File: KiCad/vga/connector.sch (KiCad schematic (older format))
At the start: 13 parts, among them J1 DB15_Female_HighDensity_Mount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, X2 Edge72

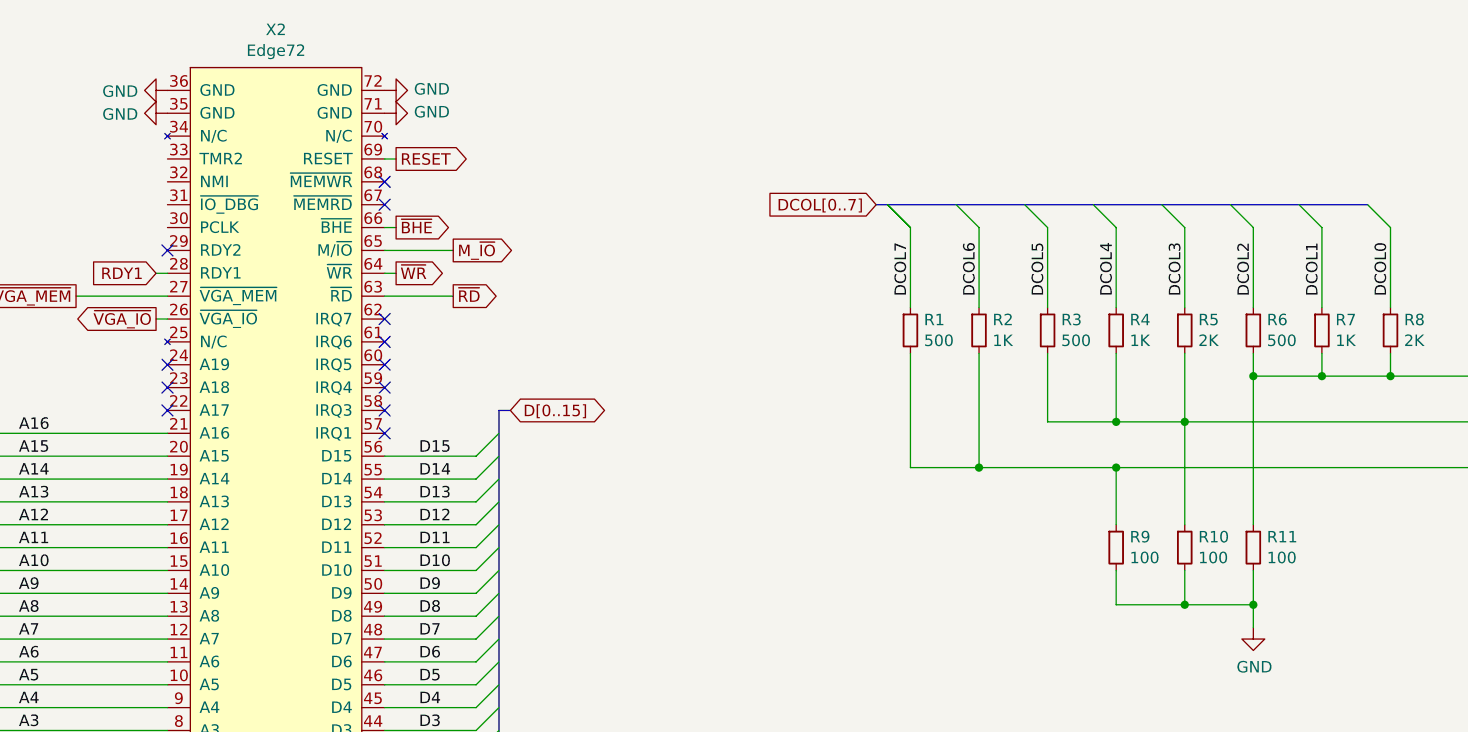
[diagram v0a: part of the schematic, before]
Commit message: Updated graphics adapter and main schematics + board.
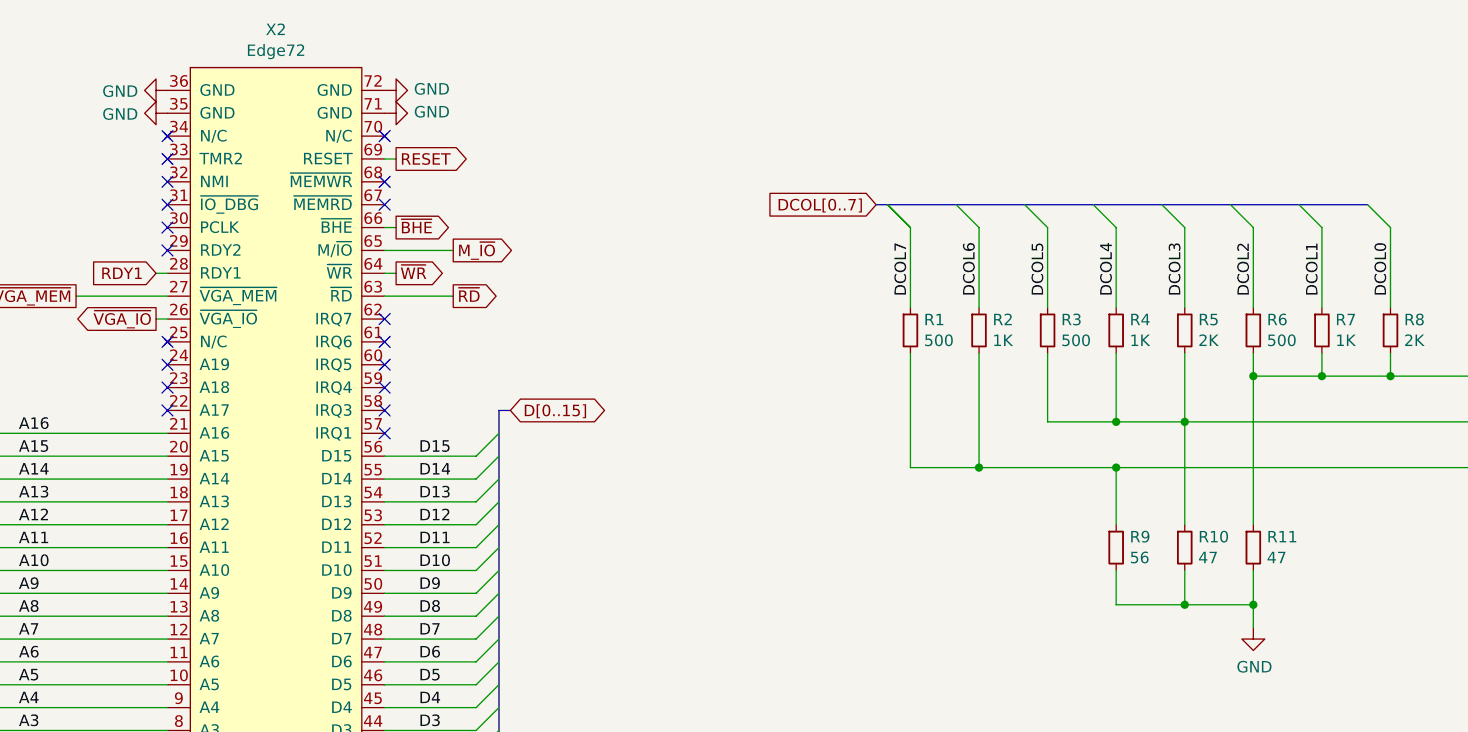
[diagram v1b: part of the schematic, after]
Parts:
- R10, R11: value 100 -> 47
- R9: value 100 -> 56
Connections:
- no-connect marks 18 -> 25
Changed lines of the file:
@@
 P 7000 4150
 F 0 "R9" H 7059 4196 50  0000 L CNN
-F 1 "100" H 7059 4105 50  0000 L CNN
+F 1 "56" H 7059 4105 50  0000 L CNN
 F 2 "Resistor_THT:R_Axial_DIN0204_L3.6mm_D1.6mm_P7.62mm_Horizontal" H 7000 4150 50  0001 C CNN
 F 3 "~" H 7000 4150 50  0001 C CNN
@@
 P 7300 4150
 F 0 "R10" H 7359 4196 50  0000 L CNN
-F 1 "100" H 7359 4105 50  0000 L CNN
+F 1 "47" H 7359 4105 50  0000 L CNN
 F 2 "Resistor_THT:R_Axial_DIN0204_L3.6mm_D1.6mm_P7.62mm_Horizontal" H 7300 4150 50  0001 C CNN
 F 3 "~" H 7300 4150 50  0001 C CNN
@@
 P 7600 4150
 F 0 "R11" H 7659 4196 50  0000 L CNN
-F 1 "100" H 7659 4105 50  0000 L CNN
+F 1 "47" H 7659 4105 50  0000 L CNN
 F 2 "Resistor_THT:R_Axial_DIN0204_L3.6mm_D1.6mm_P7.62mm_Horizontal" H 7600 4150 50  0001 C CNN
 F 3 "~" H 7600 4150 50  0001 C CNN
@@
 	1    0    0    -1
 $EndComp
-Wire Bus Line
-	5950 2650 8100 2650
-Wire Bus Line
-	2000 3400 2000 5150
-Wire Bus Line
-	4300 3550 4300 5150
 $Comp
 L Mini8086:Edge72 X2
 U 1 1 5F76D50A
 P 3300 3850
+AR Path="/5F76D50A" Ref="X2"  Part="1"
+AR Path="/5FB1662F/5F76D50A" Ref="X2"  Part="1"
 F 0 "X2" H 3325 5815 50  0000 C CNN
 F 1 "Edge72" H 3325 5724 50  0000 C CNN
@@
 	1    0    0    -1
 $EndComp
+NoConn ~ 2850 3250
+NoConn ~ 2850 2750
+NoConn ~ 2850 2650
+NoConn ~ 2850 2550
+NoConn ~ 2850 2450
+NoConn ~ 2850 2350
+NoConn ~ 3800 2350
+Wire Bus Line
+	5950 2650 8100 2650
+Wire Bus Line
+	2000 3400 2000 5150
+Wire Bus Line
+	4300 3550 4300 5150
 $EndSCHEMATC

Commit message: Updated KiCad VGA board and main board.
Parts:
- added U20: 74HC04, Package_SO:SO-14_5.3x10.2mm_P1.27mm, symbol 74xx:74HC04
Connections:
- net labels added: IRQ5, ~RESET
- net labels removed: M_~IO, RESET
- wire segments 83 -> 86
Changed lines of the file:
@@
 Text GLabel 3850 2750 2    50   Output ~ 0
 ~BHE
-Text GLabel 4100 2850 2    50   Output ~ 0
-M_~IO
 Text GLabel 3850 2950 2    50   Output ~ 0
 ~WR
@@
 ~RD
 Wire Wire Line
-	4100 2850 3800 2850
-Wire Wire Line
 	3800 3050 4100 3050
-Text GLabel 3850 2450 2    50   Output ~ 0
-RESET
 Entry Wire Line
 	4300 5150 4200 5250
@@
 Wire Wire Line
 	3850 2750 3800 2750
-Wire Wire Line
-	3800 2450 3850 2450
 Text GLabel 1950 3400 0    50   Output ~ 0
 A[0..19]
@@
 NoConn ~ 3800 3550
 NoConn ~ 3800 3450
-NoConn ~ 3800 3350
 NoConn ~ 3800 3250
 NoConn ~ 3800 3150
@@
 	1    0    0    -1
 $EndComp
-$Comp
-L Mini8086:Edge72 X2
-U 1 1 5F76D50A
-P 3300 3850
-AR Path="/5F76D50A" Ref="X2"  Part="1"
-AR Path="/5FB1662F/5F76D50A" Ref="X2"  Part="1"
-F 0 "X2" H 3325 5815 50  0000 C CNN
-F 1 "Edge72" H 3325 5724 50  0000 C CNN
-F 2 "Mini8086:BUS_72" H 3850 3850 50  0001 C CNN
-F 3 "" H 3850 3850 50  0001 C CNN
-	1    3300 3850
-	1    0    0    -1
-$EndComp
 NoConn ~ 2850 3250
 NoConn ~ 2850 2750
@@
 NoConn ~ 2850 2350
 NoConn ~ 3800 2350
+$Comp
+L Mini8086:Edge72 X2
+U 1 1 5F84BE1E
+P 3300 3850
+F 0 "X2" H 3325 5815 50  0000 C CNN
+F 1 "Edge72" H 3325 5724 50  0000 C CNN
+F 2 "Mini8086:BUS_72" H 3850 3850 50  0001 C CNN
+F 3 "" H 3850 3850 50  0001 C CNN
+	1    3300 3850
+	1    0    0    -1
+$EndComp
+Wire Wire Line
+	3800 3350 3850 3350
+Text GLabel 3850 3350 2    50   Input ~ 0
+IRQ5
+NoConn ~ 3800 2850
+$Comp
+L 74xx:74HC04 U20
+U 1 1 5F834415
+P 4550 2050
+F 0 "U20" V 4596 1870 50  0000 R CNN
+F 1 "74HC04" V 4505 1870 50  0000 R CNN
+F 2 "Package_SO:SO-14_5.3x10.2mm_P1.27mm" H 4550 2050 50  0001 C CNN
+F 3 "https://assets.nexperia.com/documents/data-sheet/74HC_HCT04.pdf" H 4550 2050 50  0001 C CNN
+	1    4550 2050
+	0    -1   -1   0
+$EndComp
+$Comp
+L 74xx:74HC04 U20
+U 2 1 5F835814
+P 1600 6650
+F 0 "U20" H 1600 6967 50  0000 C CNN
+F 1 "74HC04" H 1600 6876 50  0000 C CNN
+F 2 "Package_SO:SO-14_5.3x10.2mm_P1.27mm" H 1600 6650 50  0001 C CNN
+F 3 "https://assets.nexperia.com/documents/data-sheet/74HC_HCT04.pdf" H 1600 6650 50  0001 C CNN
+	2    1600 6650
+	1    0    0    -1
+$EndComp
+$Comp
+L 74xx:74HC04 U20
+U 3 1 5F835EDF
+P 1600 7150
+F 0 "U20" H 1600 7467 50  0000 C CNN
+F 1 "74HC04" H 1600 7376 50  0000 C CNN
+F 2 "Package_SO:SO-14_5.3x10.2mm_P1.27mm" H 1600 7150 50  0001 C CNN
+F 3 "https://assets.nexperia.com/documents/data-sheet/74HC_HCT04.pdf" H 1600 7150 50  0001 C CNN
+	3    1600 7150
+	1    0    0    -1
+$EndComp
+$Comp
+L 74xx:74HC04 U20
+U 4 1 5F836C82
+P 2650 6650
+F 0 "U20" H 2650 6967 50  0000 C CNN
+F 1 "74HC04" H 2650 6876 50  0000 C CNN
+F 2 "Package_SO:SO-14_5.3x10.2mm_P1.27mm" H 2650 6650 50  0001 C CNN
+F 3 "https://assets.nexperia.com/documents/data-sheet/74HC_HCT04.pdf" H 2650 6650 50  0001 C CNN
+	4    2650 6650
+	1    0    0    -1
+$EndComp
+$Comp
+L 74xx:74HC04 U20
+U 5 1 5F837B15
+P 2650 7150
+F 0 "U20" H 2650 7467 50  0000 C CNN
+F 1 "74HC04" H 2650 7376 50  0000 C CNN
+F 2 "Package_SO:SO-14_5.3x10.2mm_P1.27mm" H 2650 7150 50  0001 C CNN
+F 3 "https://assets.nexperia.com/documents/data-sheet/74HC_HCT04.pdf" H 2650 7150 50  0001 C CNN
+	5    2650 7150
+	1    0    0    -1
+$EndComp
+$Comp
+L 74xx:74HC04 U20
+U 6 1 5F838924
+P 3700 6650
+F 0 "U20" H 3700 6967 50  0000 C CNN
+F 1 "74HC04" H 3700 6876 50  0000 C CNN
+F 2 "Package_SO:SO-14_5.3x10.2mm_P1.27mm" H 3700 6650 50  0001 C CNN
+F 3 "https://assets.nexperia.com/documents/data-sheet/74HC_HCT04.pdf" H 3700 6650 50  0001 C CNN
+	6    3700 6650
+	1    0    0    -1
+$EndComp
+Wire Wire Line
+	4550 2450 4550 2350
+Wire Wire Line
+	3800 2450 4550 2450
+Wire Wire Line
+	4550 1750 4550 1600
+Wire Wire Line
+	4550 1600 4250 1600
+Text GLabel 4250 1600 0    50   Output ~ 0
+~RESET
+$Comp
+L power:GND #PWR089
+U 1 1 5F84397A
+P 1300 7150
+F 0 "#PWR089" H 1300 6900 50  0001 C CNN
+F 1 "GND" H 1305 6977 50  0000 C CNN
+F 2 "" H 1300 7150 50  0001 C CNN
+F 3 "" H 1300 7150 50  0001 C CNN
+	1    1300 7150
+	0    1    1    0
+$EndComp
+$Comp
+L power:GND #PWR088
+U 1 1 5F846DBC
+P 1300 6650
+F 0 "#PWR088" H 1300 6400 50  0001 C CNN
+F 1 "GND" H 1305 6477 50  0000 C CNN
+F 2 "" H 1300 6650 50  0001 C CNN
+F 3 "" H 1300 6650 50  0001 C CNN
+	1    1300 6650
+	0    1    1    0
+$EndComp
+$Comp
+L power:GND #PWR090
+U 1 1 5F847016
+P 2350 6650
+F 0 "#PWR090" H 2350 6400 50  0001 C CNN
+F 1 "GND" H 2355 6477 50  0000 C CNN
+F 2 "" H 2350 6650 50  0001 C CNN
+F 3 "" H 2350 6650 50  0001 C CNN
+	1    2350 6650
+	0    1    1    0
+$EndComp
+$Comp
+L power:GND #PWR091
+U 1 1 5F8472D3
+P 2350 7150
+F 0 "#PWR091" H 2350 6900 50  0001 C CNN
+F 1 "GND" H 2355 6977 50  0000 C CNN
+F 2 "" H 2350 7150 50  0001 C CNN
+F 3 "" H 2350 7150 50  0001 C CNN
+	1    2350 7150
+	0    1    1    0
+$EndComp
+$Comp
+L power:GND #PWR092
+U 1 1 5F847594
+P 3400 6650
+F 0 "#PWR092" H 3400 6400 50  0001 C CNN
+F 1 "GND" H 3405 6477 50  0000 C CNN
+F 2 "" H 3400 6650 50  0001 C CNN
+F 3 "" H 3400 6650 50  0001 C CNN
+	1    3400 6650
+	0    1    1    0
+$EndComp
 Wire Bus Line
 	5950 2650 8100 2650
 Wire Bus Line
+	4300 3550 4300 5150
+Wire Bus Line
 	2000 3400 2000 5150
-Wire Bus Line
-	4300 3550 4300 5150
 $EndSCHEMATC

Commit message: Updated graphics adapter
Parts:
- removed U20: 74HC04, Package_SO:SO-14_5.3x10.2mm_P1.27mm, symbol 74xx:74HC04
- added U20: 74HC00, Package_DIP:DIP-14_W7.62mm_LongPads, symbol 74xx:74HC00
- J1: value DB15_Female_HighDensity_MountingHoles -> VGA connector
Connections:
- net labels added: HSYNC, PCLK, RESET, VSYNC
- net labels removed: ~H_SYNC, ~V_SYNC
- wire segments 86 -> 100
- no-connect marks 25 -> 27
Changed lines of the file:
@@
 P 9450 3800
 F 0 "J1" H 9450 4667 50  0000 C CNN
-F 1 "DB15_Female_HighDensity_MountingHoles" H 9450 4576 50  0000 C CNN
+F 1 "VGA connector" H 9450 4576 50  0000 C CNN
 F 2 "Connector_Dsub:DSUB-15-HD_Female_Horizontal_P2.29x1.98mm_EdgePinOffset3.03mm_Housed_MountingHolesOffset4.94mm" H 8500 4200 50  0001 C CNN
 F 3 " ~" H 8500 4200 50  0001 C CNN
@@
 $EndComp
 Text GLabel 9750 3800 2    50   Input ~ 0
-~H_SYNC
+HSYNC
 Text GLabel 9750 4000 2    50   Input ~ 0
-~V_SYNC
+VSYNC
 Text Label 8850 3400 2    50   ~ 0
 R
@@
 $EndComp
 NoConn ~ 2850 3250
-NoConn ~ 2850 2750
 NoConn ~ 2850 2650
 NoConn ~ 2850 2550
@@
 IRQ5
 NoConn ~ 3800 2850
-$Comp
-L 74xx:74HC04 U20
-U 1 1 5F834415
-P 4550 2050
-F 0 "U20" V 4596 1870 50  0000 R CNN
-F 1 "74HC04" V 4505 1870 50  0000 R CNN
-F 2 "Package_SO:SO-14_5.3x10.2mm_P1.27mm" H 4550 2050 50  0001 C CNN
-F 3 "https://assets.nexperia.com/documents/data-sheet/74HC_HCT04.pdf" H 4550 2050 50  0001 C CNN
-	1    4550 2050
-	0    -1   -1   0
-$EndComp
-$Comp
-L 74xx:74HC04 U20
-U 2 1 5F835814
-P 1600 6650
-F 0 "U20" H 1600 6967 50  0000 C CNN
-F 1 "74HC04" H 1600 6876 50  0000 C CNN
-F 2 "Package_SO:SO-14_5.3x10.2mm_P1.27mm" H 1600 6650 50  0001 C CNN
-F 3 "https://assets.nexperia.com/documents/data-sheet/74HC_HCT04.pdf" H 1600 6650 50  0001 C CNN
-	2    1600 6650
-	1    0    0    -1
-$EndComp
-$Comp
-L 74xx:74HC04 U20
-U 3 1 5F835EDF
-P 1600 7150
-F 0 "U20" H 1600 7467 50  0000 C CNN
-F 1 "74HC04" H 1600 7376 50  0000 C CNN
-F 2 "Package_SO:SO-14_5.3x10.2mm_P1.27mm" H 1600 7150 50  0001 C CNN
-F 3 "https://assets.nexperia.com/documents/data-sheet/74HC_HCT04.pdf" H 1600 7150 50  0001 C CNN
-	3    1600 7150
-	1    0    0    -1
-$EndComp
-$Comp
-L 74xx:74HC04 U20
-U 4 1 5F836C82
-P 2650 6650
-F 0 "U20" H 2650 6967 50  0000 C CNN
-F 1 "74HC04" H 2650 6876 50  0000 C CNN
-F 2 "Package_SO:SO-14_5.3x10.2mm_P1.27mm" H 2650 6650 50  0001 C CNN
-F 3 "https://assets.nexperia.com/documents/data-sheet/74HC_HCT04.pdf" H 2650 6650 50  0001 C CNN
-	4    2650 6650
-	1    0    0    -1
-$EndComp
-$Comp
-L 74xx:74HC04 U20
-U 5 1 5F837B15
-P 2650 7150
-F 0 "U20" H 2650 7467 50  0000 C CNN
-F 1 "74HC04" H 2650 7376 50  0000 C CNN
-F 2 "Package_SO:SO-14_5.3x10.2mm_P1.27mm" H 2650 7150 50  0001 C CNN
-F 3 "https://assets.nexperia.com/documents/data-sheet/74HC_HCT04.pdf" H 2650 7150 50  0001 C CNN
-	5    2650 7150
-	1    0    0    -1
-$EndComp
-$Comp
-L 74xx:74HC04 U20
-U 6 1 5F838924
-P 3700 6650
-F 0 "U20" H 3700 6967 50  0000 C CNN
-F 1 "74HC04" H 3700 6876 50  0000 C CNN
-F 2 "Package_SO:SO-14_5.3x10.2mm_P1.27mm" H 3700 6650 50  0001 C CNN
-F 3 "https://assets.nexperia.com/documents/data-sheet/74HC_HCT04.pdf" H 3700 6650 50  0001 C CNN
-	6    3700 6650
-	1    0    0    -1
-$EndComp
-Wire Wire Line
-	4550 2450 4550 2350
-Wire Wire Line
-	3800 2450 4550 2450
+Wire Wire Line
+	4450 2450 4450 2350
+Wire Wire Line
+	3800 2450 4450 2450
 Wire Wire Line
 	4550 1750 4550 1600
@@
 ~RESET
 $Comp
+L 74xx:74HC00 U20
+U 1 1 5FA187DD
+P 4550 2050
+F 0 "U20" V 4596 1870 50  0000 R CNN
+F 1 "74HC00" V 4505 1870 50  0000 R CNN
+F 2 "Package_DIP:DIP-14_W7.62mm_LongPads" H 4550 2050 50  0001 C CNN
+F 3 "http://www.ti.com/lit/gpn/sn74hc00" H 4550 2050 50  0001 C CNN
+	1    4550 2050
+	0    -1   -1   0
+$EndComp
+$Comp
+L 74xx:74HC00 U20
+U 2 1 5FA19BE3
+P 3950 6600
+F 0 "U20" H 3950 6925 50  0000 C CNN
+F 1 "74HC00" H 3950 6834 50  0000 C CNN
+F 2 "Package_DIP:DIP-14_W7.62mm_LongPads" H 3950 6600 50  0001 C CNN
+F 3 "http://www.ti.com/lit/gpn/sn74hc00" H 3950 6600 50  0001 C CNN
+	2    3950 6600
+	1    0    0    -1
+$EndComp
+$Comp
+L 74xx:74HC00 U20
+U 3 1 5FA1AA9F
+P 3150 6600
+F 0 "U20" H 3150 6925 50  0000 C CNN
+F 1 "74HC00" H 3150 6834 50  0000 C CNN
+F 2 "Package_DIP:DIP-14_W7.62mm_LongPads" H 3150 6600 50  0001 C CNN
+F 3 "http://www.ti.com/lit/gpn/sn74hc00" H 3150 6600 50  0001 C CNN
+	3    3150 6600
+	1    0    0    -1
+$EndComp
+$Comp
+L 74xx:74HC00 U20
+U 4 1 5FA1C152
+P 4750 6600
+F 0 "U20" H 4750 6925 50  0000 C CNN
+F 1 "74HC00" H 4750 6834 50  0000 C CNN
+F 2 "Package_DIP:DIP-14_W7.62mm_LongPads" H 4750 6600 50  0001 C CNN
+F 3 "http://www.ti.com/lit/gpn/sn74hc00" H 4750 6600 50  0001 C CNN
+	4    4750 6600
+	1    0    0    -1
+$EndComp
+$Comp
+L 74xx:74HC00 U20
+U 5 1 5FA1CEFE
+P 5450 6600
+F 0 "U20" H 5680 6646 50  0000 L CNN
+F 1 "74HC00" H 5680 6555 50  0000 L CNN
+F 2 "Package_DIP:DIP-14_W7.62mm_LongPads" H 5450 6600 50  0001 C CNN
+F 3 "http://www.ti.com/lit/gpn/sn74hc00" H 5450 6600 50  0001 C CNN
+	5    5450 6600
+	1    0    0    -1
+$EndComp
+Wire Wire Line
+	5450 7200 4450 7200
+Wire Wire Line
+	2850 7200 2850 6700
+Connection ~ 2850 6700
+Wire Wire Line
+	2850 6700 2850 6500
+Wire Wire Line
+	3650 6500 3650 6700
+Connection ~ 3650 7200
+Wire Wire Line
+	3650 7200 2850 7200
+Connection ~ 3650 6700
+Wire Wire Line
+	3650 6700 3650 7200
+Wire Wire Line
+	4450 6500 4450 6700
+Connection ~ 4450 7200
+Wire Wire Line
+	4450 7200 3650 7200
+Connection ~ 4450 6700
+Wire Wire Line
+	4450 6700 4450 7200
+Wire Wire Line
+	5450 7300 5450 7200
+Connection ~ 5450 7200
+Wire Wire Line
+	5450 7200 5450 7100
+$Comp
 L power:GND #PWR089
-U 1 1 5F84397A
-P 1300 7150
-F 0 "#PWR089" H 1300 6900 50  0001 C CNN
-F 1 "GND" H 1305 6977 50  0000 C CNN
-F 2 "" H 1300 7150 50  0001 C CNN
-F 3 "" H 1300 7150 50  0001 C CNN
-	1    1300 7150
-	0    1    1    0
-$EndComp
-$Comp
-L power:GND #PWR088
-U 1 1 5F846DBC
-P 1300 6650
-F 0 "#PWR088" H 1300 6400 50  0001 C CNN
-F 1 "GND" H 1305 6477 50  0000 C CNN
-F 2 "" H 1300 6650 50  0001 C CNN
-F 3 "" H 1300 6650 50  0001 C CNN
-	1    1300 6650
-	0    1    1    0
-$EndComp
-$Comp
-L power:GND #PWR090
-U 1 1 5F847016
-P 2350 6650
-F 0 "#PWR090" H 2350 6400 50  0001 C CNN
-F 1 "GND" H 2355 6477 50  0000 C CNN
-F 2 "" H 2350 6650 50  0001 C CNN
-F 3 "" H 2350 6650 50  0001 C CNN
-	1    2350 6650
-	0    1    1    0
-$EndComp
-$Comp
-L power:GND #PWR091
-U 1 1 5F8472D3
-P 2350 7150
-F 0 "#PWR091" H 2350 6900 50  0001 C CNN
-F 1 "GND" H 2355 6977 50  0000 C CNN
-F 2 "" H 2350 7150 50  0001 C CNN
-F 3 "" H 2350 7150 50  0001 C CNN
-	1    2350 7150
-	0    1    1    0
-$EndComp
-$Comp
-L power:GND #PWR092
-U 1 1 5F847594
-P 3400 6650
-F 0 "#PWR092" H 3400 6400 50  0001 C CNN
-F 1 "GND" H 3405 6477 50  0000 C CNN
-F 2 "" H 3400 6650 50  0001 C CNN
-F 3 "" H 3400 6650 50  0001 C CNN
-	1    3400 6650
-	0    1    1    0
-$EndComp
+U 1 1 5FA2E1BD
+P 5450 7300
+F 0 "#PWR089" H 5450 7050 50  0001 C CNN
+F 1 "GND" H 5455 7127 50  0000 C CNN
+F 2 "" H 5450 7300 50  0001 C CNN
+F 3 "" H 5450 7300 50  0001 C CNN
+	1    5450 7300
+	1    0    0    -1
+$EndComp
+$Comp
+L power:VCC #PWR088
+U 1 1 5FA2E7CE
+P 5450 6100
+F 0 "#PWR088" H 5450 5950 50  0001 C CNN
+F 1 "VCC" H 5465 6273 50  0000 C CNN
+F 2 "" H 5450 6100 50  0001 C CNN
+F 3 "" H 5450 6100 50  0001 C CNN
+	1    5450 6100
+	1    0    0    -1
+$EndComp
+Wire Wire Line
+	4650 2350 4650 2450
+Wire Wire Line
+	4650 2450 4450 2450
+Connection ~ 4450 2450
+Text Label 4050 2450 0    50   ~ 0
+RESET
+NoConn ~ 5050 6600
+NoConn ~ 4250 6600
+NoConn ~ 3450 6600
+Wire Wire Line
+	2800 2750 2850 2750
+Text GLabel 2800 2750 0    50   Output ~ 0
+PCLK
 Wire Bus Line
 	5950 2650 8100 2650
